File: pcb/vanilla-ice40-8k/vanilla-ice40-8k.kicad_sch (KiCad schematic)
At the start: 17 parts, among them J1 QSH-060-01-L-D-A, J2 QSH-060-01-L-D-A, J3 QTH-060-01-L-D-A, J4 QTH-060-01-L-D-A, U1 ICE40HX8K-CT256, X1 SG-8101CE 100Mhz

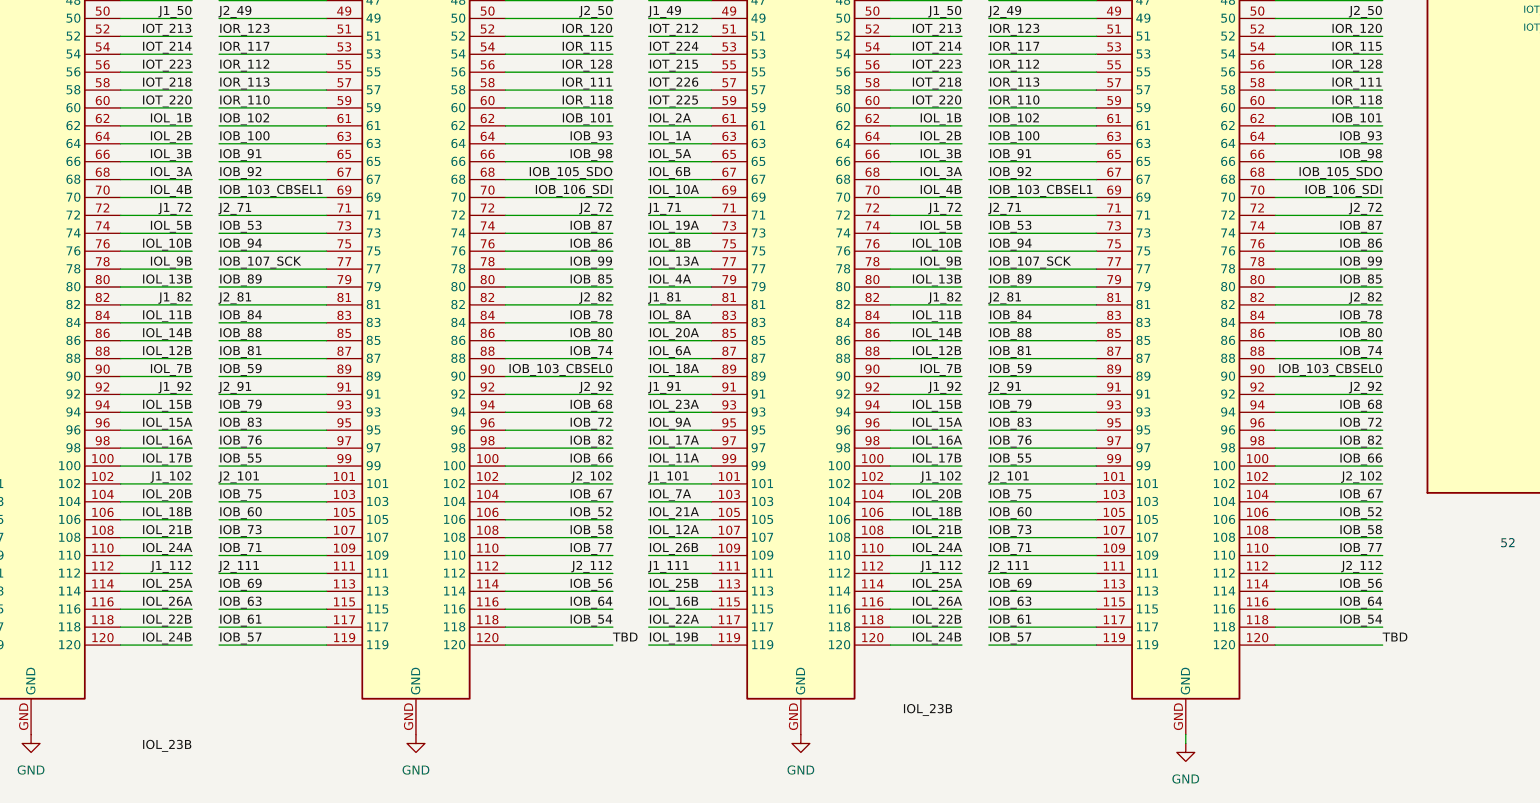
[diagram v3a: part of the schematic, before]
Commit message: [hx8k][pcb] j2 sig2 routed
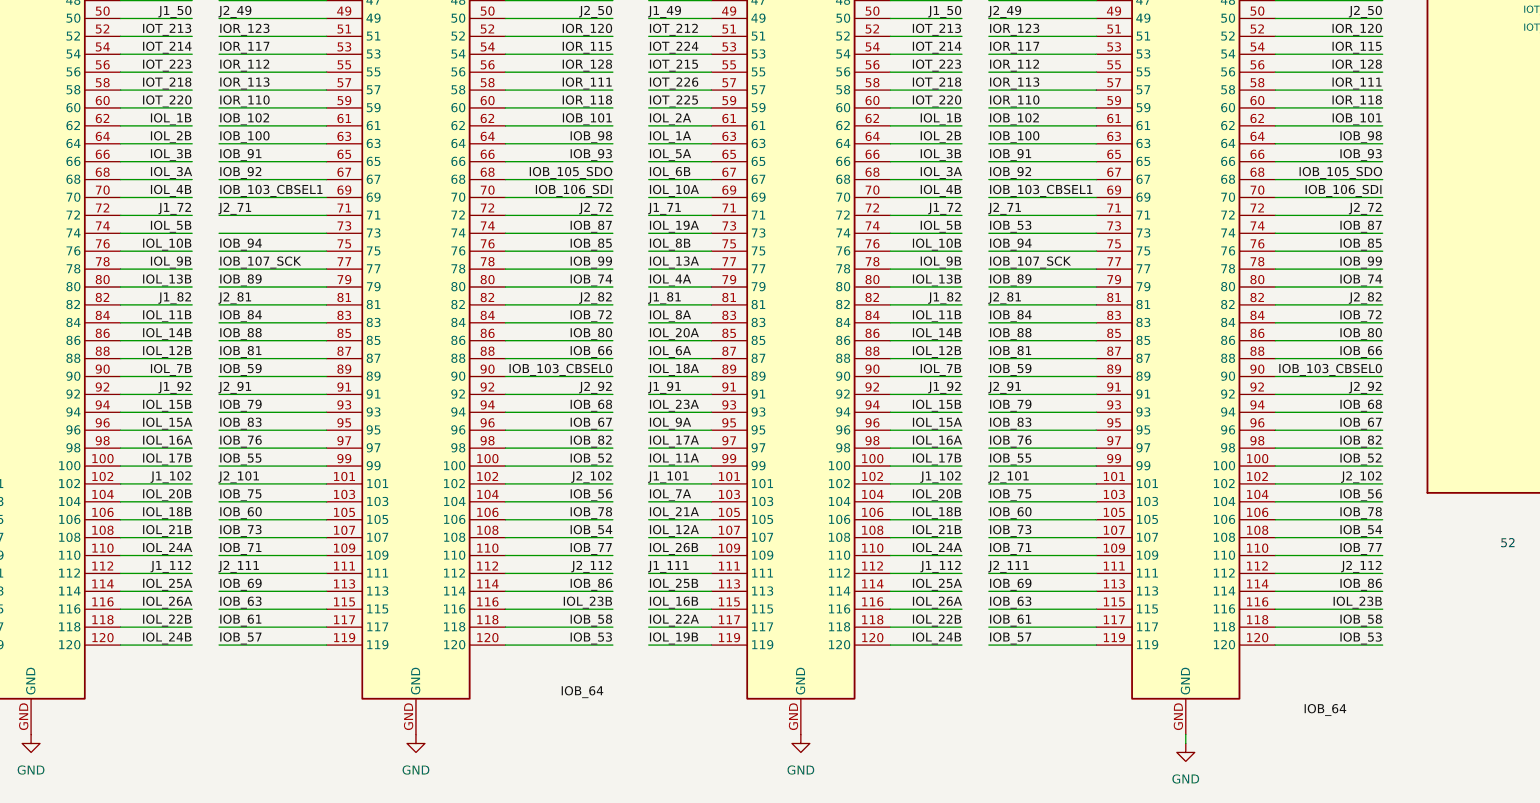
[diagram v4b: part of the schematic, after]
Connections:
- net TBD is gone; now on net IOB_53: J2.120, J4.120
- net IOB_52: now also J2.100, J4.100; no longer J2.106, J4.106
- net IOB_53: no longer J2.73
- net IOB_54: now also J2.108, J4.108; no longer J2.118, J4.118
- net IOB_56: now also J2.104, J4.104; no longer J2.114, J4.114
- net IOB_58: now also J2.118, J4.118; no longer J2.108, J4.108
- net IOB_64: no longer J2.116, J4.116
- net IOB_66: now also J2.88, J4.88; no longer J2.100, J4.100
- net IOB_67: now also J2.96, J4.96; no longer J2.104, J4.104
- net IOB_72: now also J2.84, J4.84; no longer J2.96, J4.96
- net IOB_74: now also J2.80, J4.80; no longer J2.88, J4.88
- net IOB_78: now also J2.106, J4.106; no longer J2.84, J4.84
- net IOB_85: now also J2.76, J4.76; no longer J2.80, J4.80
- net IOB_86: now also J2.114, J4.114; no longer J2.76, J4.76
- net IOB_93: now also J2.66, J4.66; no longer J2.64, J4.64
- net IOB_98: now also J2.64, J4.64; no longer J2.66, J4.66
- net IOL_23B: now also J2.116, J4.116
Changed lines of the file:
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@@
 	)
 	(label "IOB_86"
-		(at 228.6 190.5 180)
+		(at 228.6 238.76 180)
 		(effects
 			(font
@@
 	)
 	(label "IOB_53"
-		(at 63.5 187.96 0)
+		(at 119.38 246.38 180)
 		(effects
 			(font
 				(size 1.27 1.27)
 			)
-			(justify left bottom)
+			(justify right bottom)
 		)
 	)
@@
 	)
 	(label "IOB_58"
-		(at 228.6 231.14 180)
+		(at 228.6 243.84 180)
 		(effects
 			(font
@@
 	)
 	(label "IOB_85"
-		(at 119.38 195.58 180)
+		(at 119.38 190.5 180)
 		(effects
 			(font
@@
 	)
 	(label "IOB_93"
-		(at 119.38 175.26 180)
+		(at 119.38 177.8 180)
 		(effects
 			(font
@@
 	)
 	(label "IOB_64"
-		(at 119.38 241.3 180)
+		(at 118.11 254 180)
 		(effects
 			(font
@@
 	)
 	(label "IOB_98"
-		(at 228.6 177.8 180)
+		(at 228.6 175.26 180)
 		(effects
 			(font
@@
 	)
 	(label "IOB_54"
-		(at 119.38 243.84 180)
+		(at 119.38 231.14 180)
 		(effects
 			(font
@@
 	)
 	(label "IOB_74"
-		(at 228.6 205.74 180)
+		(at 228.6 195.58 180)
 		(effects
 			(font
@@
 	)
 	(label "IOB_93"
-		(at 228.6 175.26 180)
+		(at 228.6 177.8 180)
 		(effects
 			(font
@@
 	)
 	(label "IOB_67"
-		(at 228.6 226.06 180)
+		(at 228.6 215.9 180)
 		(effects
 			(font
@@
 	)
 	(label "IOB_66"
-		(at 119.38 220.98 180)
+		(at 119.38 205.74 180)
 		(effects
 			(font
@@
 	)
 	(label "IOL_23B"
-		(at 59.69 261.62 180)
+		(at 119.38 241.3 180)
 		(effects
 			(font
@@
 		)
 	)
+	(label "IOB_53"
+		(at 228.6 246.38 180)
+		(effects
+			(font
+				(size 1.27 1.27)
+			)
+			(justify right bottom)
+		)
+	)
 	(label "IOR_130"
 		(at 63.5 127 0)
@@
 	)
 	(label "IOB_78"
-		(at 228.6 200.66 180)
+		(at 228.6 228.6 180)
 		(effects
 			(font
@@
 		)
 	)
-	(label "TBD"
-		(at 119.38 246.38 0)
-		(effects
-			(font
-				(size 1.27 1.27)
-			)
-			(justify left bottom)
-		)
-	)
 	(label "IOL_16B"
 		(at 15.24 241.3 0)
@@
 	)
 	(label "IOB_66"
-		(at 228.6 220.98 180)
+		(at 228.6 205.74 180)
 		(effects
 			(font
@@
 	)
 	(label "IOB_64"
-		(at 228.6 241.3 180)
+		(at 223.52 256.54 180)
 		(effects
 			(font
@@
 	)
 	(label "IOB_52"
-		(at 228.6 228.6 180)
+		(at 228.6 220.98 180)
 		(effects
 			(font
@@
 		)
 	)
-	(label "TBD"
-		(at 228.6 246.38 0)
-		(effects
-			(font
-				(size 1.27 1.27)
-			)
-			(justify left bottom)
-		)
-	)
 	(label "IOR_111"
 		(at 325.12 97.79 180)
@@
 	)
 	(label "IOB_74"
-		(at 119.38 205.74 180)
+		(at 119.38 195.58 180)
 		(effects
 			(font
@@
 	)
 	(label "IOB_52"
-		(at 119.38 228.6 180)
+		(at 119.38 220.98 180)
 		(effects
 			(font
@@
 	)
 	(label "IOB_67"
-		(at 119.38 226.06 180)
+		(at 119.38 215.9 180)
 		(effects
 			(font
@@
 	)
 	(label "IOB_98"
-		(at 119.38 177.8 180)
+		(at 119.38 175.26 180)
 		(effects
 			(font
@@
 	)
 	(label "IOL_23B"
-		(at 167.64 256.54 180)
+		(at 228.6 241.3 180)
 		(effects
 			(font
@@
 	)
 	(label "IOB_54"
-		(at 228.6 243.84 180)
+		(at 228.6 231.14 180)
 		(effects
 			(font
@@
 	)
 	(label "IOB_72"
-		(at 228.6 215.9 180)
+		(at 228.6 200.66 180)
 		(effects
 			(font
@@
 	)
 	(label "IOB_56"
-		(at 119.38 238.76 180)
+		(at 119.38 226.06 180)
 		(effects
 			(font
@@
 	)
 	(label "IOB_85"
-		(at 228.6 195.58 180)
+		(at 228.6 190.5 180)
 		(effects
 			(font
@@
 	)
 	(label "IOB_72"
-		(at 119.38 215.9 180)
+		(at 119.38 200.66 180)
 		(effects
 			(font
@@
 	)
 	(label "IOB_86"
-		(at 119.38 190.5 180)
+		(at 119.38 238.76 180)
 		(effects
 			(font
@@
 	)
 	(label "IOB_56"
-		(at 228.6 238.76 180)
+		(at 228.6 226.06 180)
 		(effects
 			(font
@@
 	)
 	(label "IOB_78"
-		(at 119.38 200.66 180)
+		(at 119.38 228.6 180)
 		(effects
 			(font
@@
 	)
 	(label "IOB_58"
-		(at 119.38 231.14 180)
+		(at 119.38 243.84 180)
 		(effects
 			(font

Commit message: [hx8k][pcb] j2 routed
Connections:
- net IOB_103_CBSEL0: now also J2.94, J4.94; no longer J2.90, J4.90
- net IOB_52: now also J2.104, J4.104; no longer J2.100, J4.100
- net IOB_53: now also J2.105, J4.105; no longer J2.120, J4.120, J4.73
- net IOB_54: now also J2.116, J4.116; no longer J2.108, J4.108
- net IOB_56: now also J2.108, J4.108; no longer J2.104, J4.104
- net IOB_60: now also J2.73, J4.73; no longer J2.105, J4.105
- net IOB_64: now also J2.114, J4.114
- net IOB_66: now also J2.96, J4.96; no longer J2.88, J4.88
- net IOB_67: now also J2.100, J4.100; no longer J2.96, J4.96
- net IOB_68: now also J2.98, J4.98; no longer J2.94, J4.94
- net IOB_72: now also J2.88, J4.88; no longer J2.84, J4.84
- net IOB_74: now also J2.84, J4.84; no longer J2.80, J4.80
- net IOB_78: now also J2.86, J4.86; no longer J2.106, J4.106
- net IOB_80: now also J2.90, J4.90; no longer J2.86, J4.86
- net IOB_82: now also J2.106, J4.106; no longer J2.98, J4.98
- net IOB_85: now also J2.80, J4.80; no longer J2.76, J4.76
- net IOB_86: now also J2.76, J4.76; no longer J2.114, J4.114
- net IOL_23B: now also J2.120, J4.120; no longer J2.116, J4.116
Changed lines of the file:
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@@
 	)
 	(label "IOB_86"
-		(at 228.6 238.76 180)
+		(at 228.6 190.5 180)
 		(effects
 			(font
@@
 	)
 	(label "IOB_53"
-		(at 119.38 246.38 180)
+		(at 63.5 228.6 0)
 		(effects
 			(font
 				(size 1.27 1.27)
 			)
-			(justify right bottom)
+			(justify left bottom)
 		)
 	)
@@
 	)
 	(label "IOB_82"
-		(at 119.38 218.44 180)
+		(at 119.38 228.6 180)
 		(effects
 			(font
@@
 	)
 	(label "IOB_85"
-		(at 119.38 190.5 180)
+		(at 119.38 195.58 180)
 		(effects
 			(font
@@
 	)
 	(label "IOB_64"
-		(at 118.11 254 180)
+		(at 119.38 238.76 180)
 		(effects
 			(font
@@
 	)
 	(label "IOB_54"
-		(at 119.38 231.14 180)
+		(at 119.38 241.3 180)
 		(effects
 			(font
@@
 	)
 	(label "IOB_74"
-		(at 228.6 195.58 180)
+		(at 228.6 200.66 180)
 		(effects
 			(font
@@
 	)
 	(label "IOB_60"
-		(at 63.5 228.6 0)
+		(at 63.5 187.96 0)
 		(effects
 			(font
@@
 	)
 	(label "IOB_67"
-		(at 228.6 215.9 180)
+		(at 228.6 220.98 180)
 		(effects
 			(font
@@
 	)
 	(label "IOB_66"
-		(at 119.38 205.74 180)
+		(at 119.38 215.9 180)
 		(effects
 			(font
@@
 		)
 	)
-	(label "IOB_53"
-		(at 172.72 187.96 0)
-		(effects
-			(font
-				(size 1.27 1.27)
-			)
-			(justify left bottom)
-		)
-	)
 	(label "IOT_206"
 		(at 276.86 171.45 180)
@@
 	)
 	(label "IOL_23B"
-		(at 119.38 241.3 180)
+		(at 119.38 246.38 180)
 		(effects
 			(font
@@
 	)
 	(label "IOB_60"
-		(at 172.72 228.6 0)
+		(at 172.72 187.96 0)
 		(effects
 			(font
@@
 	)
 	(label "IOB_53"
-		(at 228.6 246.38 180)
+		(at 172.72 228.6 0)
 		(effects
 			(font
 				(size 1.27 1.27)
 			)
-			(justify right bottom)
+			(justify left bottom)
 		)
 	)
@@
 	)
 	(label "IOB_78"
-		(at 228.6 228.6 180)
+		(at 228.6 203.2 180)
 		(effects
 			(font
@@
 	)
 	(label "IOB_80"
-		(at 228.6 203.2 180)
+		(at 228.6 208.28 180)
 		(effects
 			(font
@@
 	)
 	(label "IOB_80"
-		(at 119.38 203.2 180)
+		(at 119.38 208.28 180)
 		(effects
 			(font
@@
 	)
 	(label "IOB_66"
-		(at 228.6 205.74 180)
+		(at 228.6 215.9 180)
 		(effects
 			(font
@@
 	)
 	(label "IOB_64"
-		(at 223.52 256.54 180)
+		(at 228.6 238.76 180)
 		(effects
 			(font
@@
 	)
 	(label "IOB_52"
-		(at 228.6 220.98 180)
+		(at 228.6 226.06 180)
 		(effects
 			(font
@@
 	)
 	(label "IOB_68"
-		(at 228.6 213.36 180)
+		(at 228.6 218.44 180)
 		(effects
 			(font
@@
 	)
 	(label "IOB_74"
-		(at 119.38 195.58 180)
+		(at 119.38 200.66 180)
 		(effects
 			(font
@@
 	)
 	(label "IOB_52"
-		(at 119.38 220.98 180)
+		(at 119.38 226.06 180)
 		(effects
 			(font
@@
 	)
 	(label "IOB_67"
-		(at 119.38 215.9 180)
+		(at 119.38 220.98 180)
 		(effects
 			(font
@@
 	)
 	(label "IOB_82"
-		(at 228.6 218.44 180)
+		(at 228.6 228.6 180)
 		(effects
 			(font
@@
 	)
 	(label "IOL_23B"
-		(at 228.6 241.3 180)
+		(at 228.6 246.38 180)
 		(effects
 			(font
@@
 	)
 	(label "IOB_54"
-		(at 228.6 231.14 180)
+		(at 228.6 241.3 180)
 		(effects
 			(font
@@
 	)
 	(label "IOB_72"
-		(at 228.6 200.66 180)
+		(at 228.6 205.74 180)
 		(effects
 			(font
@@
 	)
 	(label "IOB_56"
-		(at 119.38 226.06 180)
+		(at 119.38 231.14 180)
 		(effects
 			(font
@@
 	)
 	(label "IOB_103_CBSEL0"
-		(at 119.38 208.28 180)
+		(at 119.38 213.36 180)
 		(effects
 			(font
@@
 	)
 	(label "IOB_85"
-		(at 228.6 190.5 180)
+		(at 228.6 195.58 180)
 		(effects
 			(font
@@
 	)
 	(label "IOB_72"
-		(at 119.38 200.66 180)
+		(at 119.38 205.74 180)
 		(effects
 			(font
@@
 	)
 	(label "IOB_103_CBSEL0"
-		(at 228.6 208.28 180)
+		(at 228.6 213.36 180)
 		(effects
 			(font
@@
 	)
 	(label "IOB_86"
-		(at 119.38 238.76 180)
+		(at 119.38 190.5 180)
 		(effects
 			(font
@@
 	)
 	(label "IOB_56"
-		(at 228.6 226.06 180)
+		(at 228.6 231.14 180)
 		(effects
 			(font
@@
 	)
 	(label "IOB_78"
-		(at 119.38 228.6 180)
+		(at 119.38 203.2 180)
 		(effects
 			(font
@@
 	)
 	(label "IOB_68"
-		(at 119.38 213.36 180)
+		(at 119.38 218.44 180)
 		(effects
 			(font

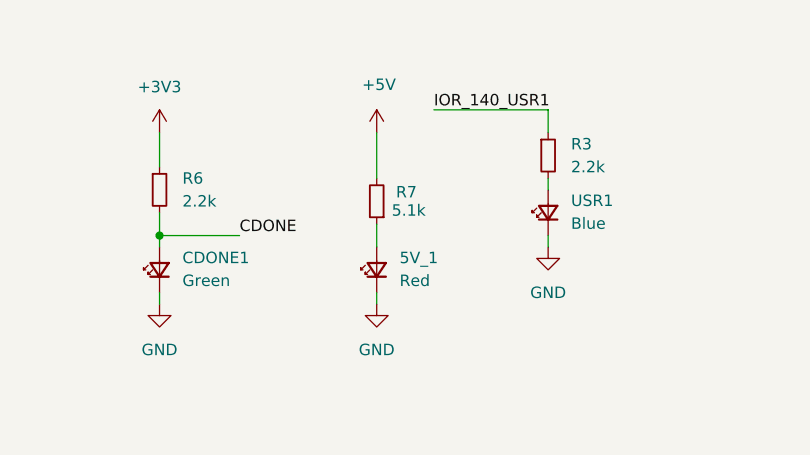
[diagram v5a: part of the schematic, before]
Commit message: [hx8k][pcb] rough layout of full board
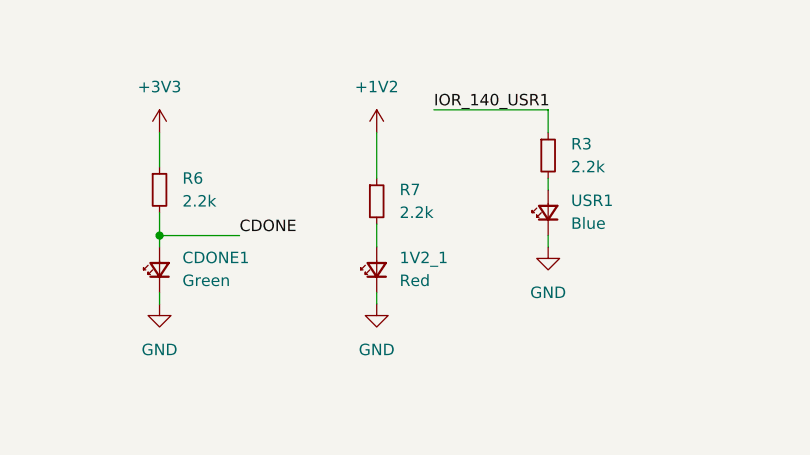
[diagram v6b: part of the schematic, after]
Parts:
- R7: value 5.1k -> 2.2k; Digi-Key Part Number CR0603-FX-5101ELFCT-ND -> 118-CR0603-FX-2201ELFCT-ND; LCSC Part # C23186 -> C4190
- renumbered 5V_1 to 1V2_1
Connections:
- net +5V is gone; now on an unnamed net: R7.2
- net at 1V2_1.2 (A): no longer R7.1
- new net +1V2: R7.1
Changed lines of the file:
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@@
+	)
+	(symbol
+		(lib_id "power:VBUS")
+		(at 309.88 27.94 0)
+		(unit 1)
+		(exclude_from_sim no)
+		(in_bom yes)
+		(on_board yes)
+		(dnp no)
+		(property "Reference" "#PWR093"
+			(at 309.88 31.75 0)
+			(effects
+				(font
+					(size 1.27 1.27)
+				)
+				(hide yes)
+			)
+		)
+		(property "Value" "+1V2"
+			(at 309.88 22.86 0)
+			(effects
+				(font
+					(size 1.27 1.27)
+				)
+			)
+		)
+		(property "Footprint" ""
+			(at 309.88 27.94 0)
+			(effects
+				(font
+					(size 1.27 1.27)
+				)
+				(hide yes)
+			)
+		)
+		(property "Datasheet" ""
+			(at 309.88 27.94 0)
+			(effects
+				(font
+					(size 1.27 1.27)
+				)
+				(hide yes)
+			)
+		)
+		(property "Description" "Power symbol creates a global label with name \"VBUS\""
+			(at 309.88 27.94 0)
+			(effects
+				(font
+					(size 1.27 1.27)
+				)
+				(hide yes)
+			)
+		)
+		(pin "1"
+		)
+		(instances
+			(project "vanilla-ice40-8k"
+				(path "/6fdfbf4b-014a-4077-8dc3-7ce5ecaf5fe5"
+					(reference "#PWR093")
+					(unit 1)
+				)
+			)
+		)
 	)
 	(symbol
@@
 	)
 	(symbol
+		(lib_id "Device:R_Small")
+		(at 309.88 35.56 0)
+		(unit 1)
+		(exclude_from_sim no)
+		(in_bom yes)
+		(on_board yes)
+		(dnp no)
+		(fields_autoplaced yes)
+		(property "Reference" "R7"
+			(at 312.42 34.2899 0)
+			(effects
+				(font
+					(size 1.27 1.27)
+				)
+				(justify left)
+			)
+		)
+		(property "Value" "2.2k"
+			(at 312.42 36.8299 0)
+			(effects
+				(font
+					(size 1.27 1.27)
+				)
+				(justify left)
+			)
+		)
+		(property "Footprint" "Resistor_SMD:R_0603_1608Metric"
+			(at 309.88 35.56 0)
+			(effects
+				(font
+					(size 1.27 1.27)
+				)
+				(hide yes)
+			)
+		)
+		(property "Datasheet" "~"
+			(at 309.88 35.56 0)
+			(effects
+				(font
+					(size 1.27 1.27)
+				)
+				(hide yes)
+			)
+		)
+		(property "Description" "Resistor, small symbol"
+			(at 309.88 35.56 0)
+			(effects
+				(font
+					(size 1.27 1.27)
+				)
+				(hide yes)
+			)
+		)
+		(property "LCSC Part #" "C4190"
+			(at 309.88 35.56 0)
+			(effects
+				(font
+					(size 1.27 1.27)
+				)
+				(hide yes)
+			)
+		)
+		(property "JLCPCB Rotation Offset" ""
+			(at 309.88 35.56 0)
+			(effects
+				(font
+					(size 1.27 1.27)
+				)
+				(hide yes)
+			)
+		)
+		(property "Digi-Key Part Number" "118-CR0603-FX-2201ELFCT-ND"
+			(at 309.88 35.56 0)
+			(effects
+				(font
+					(size 1.27 1.27)
+				)
+				(hide yes)
+			)
+		)
+		(pin "2"
+		)
+		(pin "1"
+		)
+		(instances
+			(project "vanilla-ice40-8k"
+				(path "/6fdfbf4b-014a-4077-8dc3-7ce5ecaf5fe5"
+					(reference "R7")
+					(unit 1)
+				)
+			)
+		)
+	)
+	(symbol
 		(lib_id "Device:C_Small")
 		(at 254 31.75 0)
@@
 				(path "/6fdfbf4b-014a-4077-8dc3-7ce5ecaf5fe5"
 					(reference "C1")
-					(unit 1)
-				)
-			)
-		)
-	)
-	(symbol
-		(lib_id "power:VBUS")
-		(at 309.88 27.94 0)
-		(unit 1)
-		(exclude_from_sim no)
-		(in_bom yes)
-		(on_board yes)
-		(dnp no)
-		(property "Reference" "#PWR06"
-			(at 309.88 31.75 0)
-			(effects
-				(font
-					(size 1.27 1.27)
-				)
-				(hide yes)
-			)
-		)
-		(property "Value" "+5V"
-			(at 310.134 22.606 0)
-			(effects
-				(font
-					(size 1.27 1.27)
-				)
-			)
-		)
-		(property "Footprint" ""
-			(at 309.88 27.94 0)
-			(effects
-				(font
-					(size 1.27 1.27)
-				)
-				(hide yes)
-			)
-		)
-		(property "Datasheet" ""
-			(at 309.88 27.94 0)
-			(effects
-				(font
-					(size 1.27 1.27)
-				)
-				(hide yes)
-			)
-		)
-		(property "Description" "Power symbol creates a global label with name \"VBUS\""
-			(at 309.88 27.94 0)
-			(effects
-				(font
-					(size 1.27 1.27)
-				)
-				(hide yes)
-			)
-		)
-		(pin "1"
-		)
-		(instances
-			(project "vanilla-ice40-8k"
-				(path "/6fdfbf4b-014a-4077-8dc3-7ce5ecaf5fe5"
-					(reference "#PWR06")
 					(unit 1)
 				)
@@
 		(on_board yes)
 		(dnp no)
-		(property "Reference" "5V_1"
+		(property "Reference" "1V2_1"
 			(at 312.42 41.8464 90)
 			(effects
@@
 			(project "vanilla-ice40-8k"
 				(path "/6fdfbf4b-014a-4077-8dc3-7ce5ecaf5fe5"
-					(reference "5V_1")
+					(reference "1V2_1")
 					(unit 1)
 				)
-			)
-		)
-	)
-	(symbol
-		(lib_id "Device:R_Small")
-		(at 309.88 35.56 180)
-		(unit 1)
-		(exclude_from_sim no)
-		(in_bom yes)
-		(on_board yes)
-		(dnp no)
-		(property "Reference" "R7"
-			(at 313.182 34.544 0)
-			(effects
-				(font
-					(size 1.27 1.27)
-				)
-			)
-		)
-		(property "Value" "5.1k"
-			(at 313.436 36.576 0)
-			(effects
-				(font
-					(size 1.27 1.27)
-				)
-			)
-		)
-		(property "Footprint" "Resistor_SMD:R_0603_1608Metric"
-			(at 309.88 35.56 0)
-			(effects
-				(font
-					(size 1.27 1.27)
-				)
-				(hide yes)
-			)
-		)
-		(property "Datasheet" "~"
-			(at 309.88 35.56 0)
-			(effects
-				(font
-					(size 1.27 1.27)
-				)
-				(hide yes)
-			)
-		)
-		(property "Description" "Resistor, small symbol"
-			(at 309.88 35.56 0)
-			(effects
-				(font
-					(size 1.27 1.27)
-				)
-				(hide yes)
-			)
-		)
-		(property "LCSC Part #" "C23186"
-			(at 309.88 35.56 0)
-			(effects
-				(font
-					(size 1.27 1.27)
-				)
-				(hide yes)
-			)
-		)
-		(property "JLCPCB Rotation Offset" ""
-			(at 309.88 35.56 0)
-			(effects
-				(font
-					(size 1.27 1.27)
-				)
-				(hide yes)
-			)
-		)
-		(property "Digi-Key Part Number" "CR0603-FX-5101ELFCT-ND"
-			(at 309.88 35.56 0)
-			(effects
-				(font
-					(size 1.27 1.27)
-				)
-				(hide yes)
-			)
-		)
-		(pin "2"
-		)
-		(pin "1"
-		)
-		(instances
-			(project "vanilla-ice40-8k"
-				(path "/6fdfbf4b-014a-4077-8dc3-7ce5ecaf5fe5"
-					(reference "R7")
-					(unit 1)
-				)

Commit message: [hx8k][pcb] rough layout improvements
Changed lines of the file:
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@@
 		)
 	)
-	(label "IOB_107_SCK"
-		(at 158.75 67.31 180)
-		(effects
-			(font
-				(size 1.27 1.27)
-			)
-			(justify right bottom)
-		)
-	)
 	(label "IOT_183"
 		(at 276.86 128.27 180)
@@
 		)
 	)
-	(label "IOR_158"
-		(at 121.92 86.36 180)
-		(effects
-			(font
-				(size 1.27 1.27)
-			)
-			(justify right bottom)
-		)
-	)
 	(label "IOR_128"
 		(at 325.12 135.89 180)
@@
 		(effects
 			(font
-				(size 1.27 1.27)
-			)
-			(justify right bottom)
-		)
-	)
-	(label "IOR_158"
-		(at 218.44 86.36 180)
-		(effects
-			(font
